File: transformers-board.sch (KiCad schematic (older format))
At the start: 51 parts, among them J1 Screw_Terminal_01x02, J2 Screw_Terminal_01x02, J3 Screw_Terminal_01x02, Q1 IRF3205, U1 UC2844NG4, U2 PC47PQ20_16Z-22

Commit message: Add layout updates
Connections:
- net GNDA: now also C21.2, C23.2; no longer C21.1, C23.1
- net VCCQ: now also C21.1, C23.1; no longer C21.2, C23.2
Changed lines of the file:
@@
 U 1 1 607D6AE4
 P 13725 3825
-F 0 "C20" H 13475 3825 50  0000 L CNN
-F 1 "EEHZA1H101P" H 13150 3925 50  0000 L CNN
+F 0 "C20" H 13450 3825 50  0000 L CNN
+F 1 "EEHZA1H101P" H 13150 3725 50  0000 L CNN
 F 2 "transformers-board:CAPAE1030X1050N" H 13763 3675 50  0001 C CNN
 F 3 "~" H 13725 3825 50  0001 C CNN
@@
 U 1 1 607E1ED3
 P 13950 3825
-F 0 "C21" H 13700 3825 50  0000 L CNN
-F 1 "EEHZA1H101P" H 13350 3725 50  0000 L CNN
+F 0 "C21" H 14075 3825 50  0000 L CNN
+F 1 "EEHZA1H101P" H 14000 3725 50  0000 L CNN
 F 2 "transformers-board:CAPAE1030X1050N" H 13988 3675 50  0001 C CNN
 F 3 "~" H 13950 3825 50  0001 C CNN
 	1    13950 3825
-	-1   0    0    1
+	1    0    0    -1
 $EndComp
 Connection ~ 625  4425
@@
 U 1 1 6082705A
 P 14825 4100
-F 0 "C23" H 14575 4100 50  0000 L CNN
-F 1 "EEHZA1H101P" H 14250 4200 50  0000 L CNN
+F 0 "C23" H 14950 4100 50  0000 L CNN
+F 1 "EEHZA1H101P" H 14850 4000 50  0000 L CNN
 F 2 "transformers-board:CAPAE1030X1050N" H 14863 3950 50  0001 C CNN
 F 3 "~" H 14825 4100 50  0001 C CNN
 	1    14825 4100
-	-1   0    0    1
+	1    0    0    -1
 $EndComp
 $Comp

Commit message: Make changes for Beat's comments
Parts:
- D2, D3, D5, D6, D7: value SL04-E3-08 -> SS2FL4-M3/H
- R7: value 0.75 -> 0.05; PurchasingLink https://www.digikey.com/products/en?keywords=RNCP0805FTD100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 -> https://www.digikey.com/en/products/detail/panasonic-electr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
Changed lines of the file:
@@
 	7000 7850 7000 7500
 Connection ~ 7000 7850
-$Comp
-L Device:D_Schottky D3
-U 1 1 6069B8B4
-P 7000 8475
-F 0 "D3" V 6954 8554 50  0000 L CNN
-F 1 "SL04-E3-08" V 7045 8554 50  0000 L CNN
-F 2 "transformers-board:SODFL3718X108N" H 7000 8475 50  0001 C CNN
-F 3 "~" H 7000 8475 50  0001 C CNN
-	1    7000 8475
-	0    1    1    0
-$EndComp
 Wire Wire Line
 	7000 8625 7000 9250
@@
 	1    7000 6625
 	1    0    0    -1
-$EndComp
-$Comp
-L Device:D_Schottky D2
-U 1 1 606A1A6E
-P 7000 7350
-F 0 "D2" V 6954 7429 50  0000 L CNN
-F 1 "SL04-E3-08" V 7045 7429 50  0000 L CNN
-F 2 "transformers-board:SODFL3718X108N" H 7000 7350 50  0001 C CNN
-F 3 "~" H 7000 7350 50  0001 C CNN
-	1    7000 7350
-	0    1    1    0
 $EndComp
 $Comp
@@
 P 9225 8725
 F 0 "R7" H 9155 8679 50  0000 R CNN
-F 1 "0.75" H 9155 8770 50  0000 R CNN
+F 1 "0.05" H 9155 8770 50  0000 R CNN
 F 2 "footprints:R_0805_OEM" H 8425 8875 50  0001 C CNN
-F 3 "https://www.seielect.com/Catalog/SEI-rncp.pdf" H 8925 9225 50  0001 C CNN
+F 3 "https://industrial.panasonic.com/cdbs/www-data/pdf/RDN0000/AOA0000C313.pdf" H 8925 9225 50  0001 C CNN
 F 4 "DK" H 9225 8725 60  0001 C CNN "MFN"
 F 5 "RNCP0805FTD100RCT-ND" H 8575 8975 60  0001 C CNN "MPN"
-F 6 "https://www.digikey.com/products/en?keywords=RNCP0805FTD100RCT-ND" H 9705 9125 60  0001 C CNN "PurchasingLink"
+F 6 "https://www.digikey.com/en/products/detail/panasonic-electronic-components/ERJ-L06KJ50MV/570932" H 9705 9125 60  0001 C CNN "PurchasingLink"
 	1    9225 8725
 	-1   0    0    1
@@
 Wire Wire Line
 	6850 5250 6850 5450
-$Comp
-L Device:D_Schottky D5
-U 1 1 606A7CB3
-P 7550 4550
-F 0 "D5" H 7600 4725 50  0000 L CNN
-F 1 "SL04-E3-08" H 7595 4629 50  0000 L CNN
-F 2 "transformers-board:SODFL3718X108N" H 7550 4550 50  0001 C CNN
-F 3 "~" H 7550 4550 50  0001 C CNN
-	1    7550 4550
-	1    0    0    -1
-$EndComp
 Wire Wire Line
 	6850 4550 7400 4550
@@
 Wire Wire Line
 	9225 3025 9225 3975
-$Comp
-L Device:D_Schottky D6
-U 1 1 606FF96B
-P 8775 3025
-F 0 "D6" H 8825 3200 50  0000 L CNN
-F 1 "SL04-E3-08" H 8820 3104 50  0000 L CNN
-F 2 "transformers-board:SODFL3718X108N" H 8775 3025 50  0001 C CNN
-F 3 "~" H 8775 3025 50  0001 C CNN
-	1    8775 3025
-	1    0    0    -1
-$EndComp
 Wire Wire Line
 	8625 3025 8250 3025
@@
 Wire Wire Line
 	625  4425 625  4625
-$Comp
-L Device:D_Schottky D7
-U 1 1 6078868E
-P 12000 3475
-F 0 "D7" H 12050 3650 50  0000 L CNN
-F 1 "SL04-E3-08" H 12045 3554 50  0000 L CNN
-F 2 "transformers-board:SODFL3718X108N" H 12000 3475 50  0001 C CNN
-F 3 "~" H 12000 3475 50  0001 C CNN
-	1    12000 3475
-	-1   0    0    1
-$EndComp
 Wire Wire Line
 	11325 3475 11850 3475
@@
 	1    0    0    -1
 $EndComp
+$Comp
+L Device:D_Schottky D7
+U 1 1 6078868E
+P 12000 3475
+F 0 "D7" H 12050 3650 50  0000 L CNN
+F 1 "SS2FL4-M3/H" H 12045 3554 50  0000 L CNN
+F 2 "transformers-board:SODFL3718X108N" H 12000 3475 50  0001 C CNN
+F 3 "https://www.vishay.com/docs/87617/ss2fl4.pdf" H 12000 3475 50  0001 C CNN
+	1    12000 3475
+	-1   0    0    1
+$EndComp
+$Comp
+L Device:D_Schottky D5
+U 1 1 6075E6CB
+P 7550 4550
+F 0 "D5" H 7600 4725 50  0000 L CNN
+F 1 "SS2FL4-M3/H" H 7595 4629 50  0000 L CNN
+F 2 "transformers-board:SODFL3718X108N" H 7550 4550 50  0001 C CNN
+F 3 "https://www.vishay.com/docs/87617/ss2fl4.pdf" H 7550 4550 50  0001 C CNN
+	1    7550 4550
+	1    0    0    -1
+$EndComp
+$Comp
+L Device:D_Schottky D6
+U 1 1 60767520
+P 8775 3025
+F 0 "D6" H 8825 3200 50  0000 L CNN
+F 1 "SS2FL4-M3/H" H 8820 3104 50  0000 L CNN
+F 2 "transformers-board:SODFL3718X108N" H 8775 3025 50  0001 C CNN
+F 3 "https://www.vishay.com/docs/87617/ss2fl4.pdf" H 8775 3025 50  0001 C CNN
+	1    8775 3025
+	1    0    0    -1
+$EndComp
+$Comp
+L Device:D_Schottky D3
+U 1 1 6077F86E
+P 7000 8475
+F 0 "D3" V 6975 8550 50  0000 L CNN
+F 1 "SS2FL4-M3/H" V 7045 8554 50  0000 L CNN
+F 2 "transformers-board:SODFL3718X108N" H 7000 8475 50  0001 C CNN
+F 3 "https://www.vishay.com/docs/87617/ss2fl4.pdf" H 7000 8475 50  0001 C CNN
+	1    7000 8475
+	0    1    1    0
+$EndComp
+$Comp
+L Device:D_Schottky D2
+U 1 1 607A001D
+P 7000 7350
+F 0 "D2" V 6975 7425 50  0000 L CNN
+F 1 "SS2FL4-M3/H" V 7045 7429 50  0000 L CNN
+F 2 "transformers-board:SODFL3718X108N" H 7000 7350 50  0001 C CNN
+F 3 "https://www.vishay.com/docs/87617/ss2fl4.pdf" H 7000 7350 50  0001 C CNN
+	1    7000 7350
+	0    1    1    0
+$EndComp
 $EndSCHEMATC

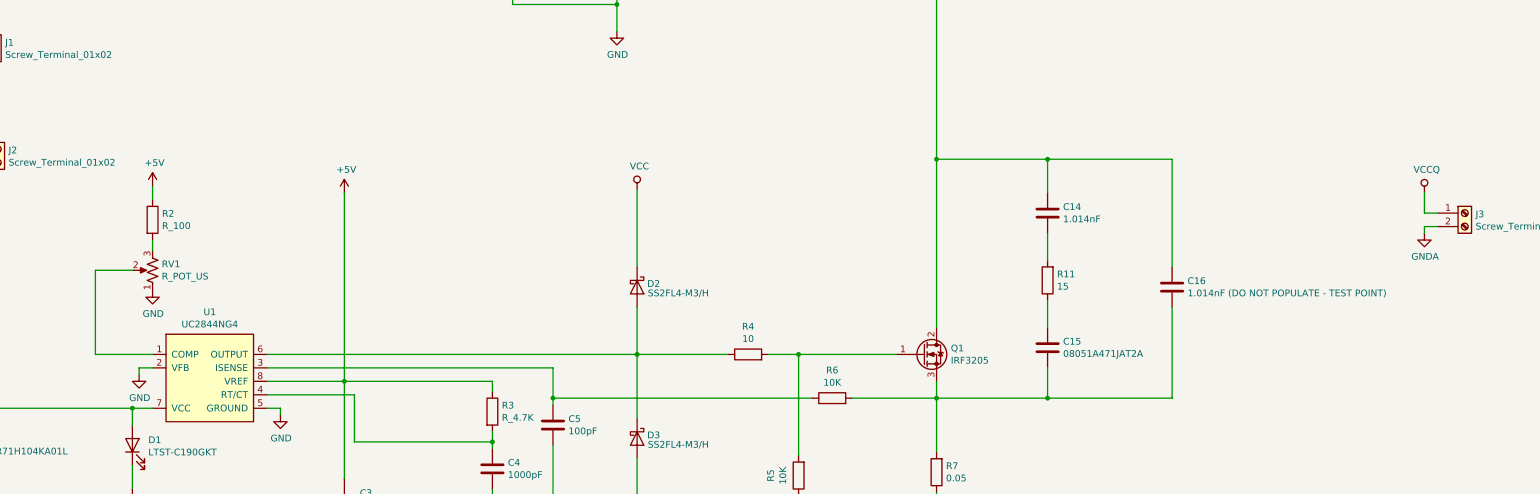
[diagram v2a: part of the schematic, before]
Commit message: Add fabrication outputs
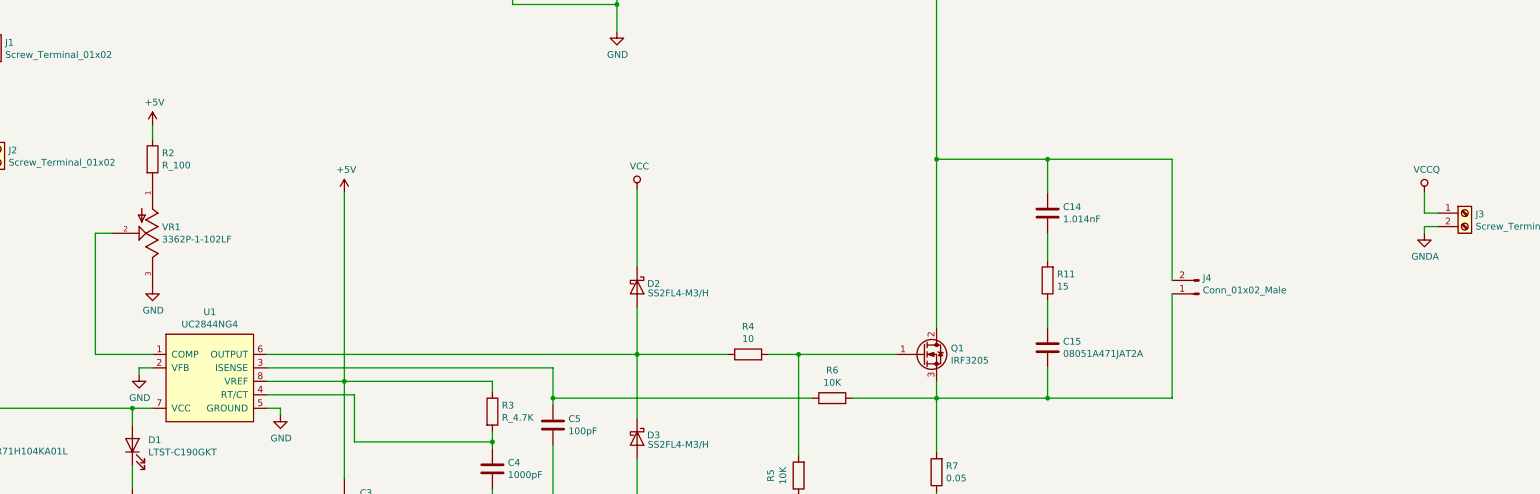
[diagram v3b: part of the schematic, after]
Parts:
- removed C16: 1.014nF (DO NOT POPULATE - TEST POINT), Connector_PinHeader_2.54mm:PinHeader_1x02_P2.54mm_Vertical, symbol Device:C
- removed RV1: R_POT_US, symbol Device:R_POT_US
- added J4: Conn_01x02_Male, Connector_PinHeader_2.54mm:PinHeader_1x02_P2.54mm_Vertical, symbol Connector:Conn_01x02_Male
- added VR1: 3362P-1-102LF, transformers-board:TRIM_3362P-1-102LF, symbol transformers-cc:3362P-1-102LF
- C12: footprint Capacitor_SMD:C_0805_2012Metric -> transformers-board:CAPAE1350X1400N
- C13: footprint Capacitor_SMD:C_0805_2012Metric -> transformers-board:CAPPRD500W60D1000H1800
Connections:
- net GND: now also VR1.3
- net at U1.1 (COMP): now also VR1.2
- net at R2.2: now also VR1.1
- net at C15.2, Q1.3 (S), R6.2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: now also J4.1 (Pin_1)
- net at C14.1, D6.2 (A), Q1.2 (D)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: now also J4.2 (Pin_2)
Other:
- moved on the sheet: R2
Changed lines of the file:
@@
 Wire Wire Line
 	3400 7850 2975 7850
-Wire Wire Line
-	2975 7850 2975 7225
-Wire Wire Line
-	2975 7225 3250 7225
 $Comp
 L power:GND #PWR09
 U 1 1 6066BB95
-P 3400 7375
-F 0 "#PWR09" H 3400 7125 50  0001 C CNN
-F 1 "GND" H 3405 7202 50  0000 C CNN
-F 2 "" H 3400 7375 50  0001 C CNN
-F 3 "" H 3400 7375 50  0001 C CNN
-	1    3400 7375
+P 3400 7350
+F 0 "#PWR09" H 3400 7100 50  0001 C CNN
+F 1 "GND" H 3405 7177 50  0000 C CNN
+F 2 "" H 3400 7350 50  0001 C CNN
+F 3 "" H 3400 7350 50  0001 C CNN
+	1    3400 7350
 	1    0    0    -1
 $EndComp
@@
 	1925 6325 2050 6325
 $Comp
-L Device:R_POT_US RV1
-U 1 1 6067D5A6
-P 3400 7225
-F 0 "RV1" H 3332 7179 50  0000 R CNN
-F 1 "R_POT_US" H 3332 7270 50  0000 R CNN
-F 2 "" H 3400 7225 50  0001 C CNN
-F 3 "~" H 3400 7225 50  0001 C CNN
-	1    3400 7225
-	-1   0    0    1
-$EndComp
-$Comp
 L rocketry:R_100 R2
 U 1 1 6067EB76
-P 3400 6850
-F 0 "R2" H 3470 6896 50  0000 L CNN
-F 1 "R_100" H 3470 6805 50  0000 L CNN
-F 2 "footprints:R_0805_OEM" H 2600 7000 50  0001 C CNN
-F 3 "https://www.seielect.com/Catalog/SEI-rncp.pdf" H 3100 7350 50  0001 C CNN
-F 4 "DK" H 3400 6850 60  0001 C CNN "MFN"
-F 5 "RNCP0805FTD100RCT-ND" H 2750 7100 60  0001 C CNN "MPN"
-F 6 "https://www.digikey.com/products/en?keywords=RNCP0805FTD100RCT-ND" H 3880 7250 60  0001 C CNN "PurchasingLink"
-	1    3400 6850
-	1    0    0    -1
-$EndComp
-Wire Wire Line
-	3400 7000 3400 7075
-Wire Wire Line
-	3400 6600 3400 6700
+P 3400 6400
+F 0 "R2" H 3470 6446 50  0000 L CNN
+F 1 "R_100" H 3470 6355 50  0000 L CNN
+F 2 "footprints:R_0805_OEM" H 2600 6550 50  0001 C CNN
+F 3 "https://www.seielect.com/Catalog/SEI-rncp.pdf" H 3100 6900 50  0001 C CNN
+F 4 "DK" H 3400 6400 60  0001 C CNN "MFN"
+F 5 "RNCP0805FTD100RCT-ND" H 2750 6650 60  0001 C CNN "MPN"
+F 6 "https://www.digikey.com/products/en?keywords=RNCP0805FTD100RCT-ND" H 3880 6800 60  0001 C CNN "PurchasingLink"
+	1    3400 6400
+	1    0    0    -1
+$EndComp
+Wire Wire Line
+	3400 6150 3400 6250
 $Comp
 L power:+5V #PWR08
 U 1 1 6067FED6
-P 3400 6600
-F 0 "#PWR08" H 3400 6450 50  0001 C CNN
-F 1 "+5V" H 3415 6773 50  0000 C CNN
-F 2 "" H 3400 6600 50  0001 C CNN
-F 3 "" H 3400 6600 50  0001 C CNN
-	1    3400 6600
+P 3400 6150
+F 0 "#PWR08" H 3400 6000 50  0001 C CNN
+F 1 "+5V" H 3415 6323 50  0000 C CNN
+F 2 "" H 3400 6150 50  0001 C CNN
+F 3 "" H 3400 6150 50  0001 C CNN
+	1    3400 6150
 	1    0    0    -1
 $EndComp
@@
 Wire Wire Line
 	10050 6400 10975 6400
-Wire Wire Line
-	10975 6400 10975 7200
 Connection ~ 10050 6400
-Wire Wire Line
-	10975 7500 10975 8175
 Wire Wire Line
 	10975 8175 10050 8175
 Connection ~ 10050 8175
-$Comp
-L Device:C C16
-U 1 1 606DF590
-P 10975 7350
-F 0 "C16" H 11090 7396 50  0000 L CNN
-F 1 "1.014nF (DO NOT POPULATE - TEST POINT)" H 11090 7305 50  0000 L CNN
-F 2 "Connector_PinHeader_2.54mm:PinHeader_1x02_P2.54mm_Vertical" H 11013 7200 50  0001 C CNN
-F 3 "~" H 10975 7350 50  0001 C CNN
-	1    10975 7350
-	1    0    0    -1
-$EndComp
 $Comp
 L Connector:Screw_Terminal_01x02 J3
@@
 F 0 "C13" H 6965 5021 50  0000 L CNN
 F 1 "120uF" H 6965 4930 50  0000 L CNN
-F 2 "Capacitor_SMD:C_0805_2012Metric" H 6888 4825 50  0001 C CNN
+F 2 "transformers-board:CAPPRD500W60D1000H1800" H 6888 4825 50  0001 C CNN
 F 3 "~" H 6850 4975 50  0001 C CNN
 	1    6850 4975
@@
 F 0 "C12" H 6965 3446 50  0000 L CNN
 F 1 "200uF" H 6965 3355 50  0000 L CNN
-F 2 "Capacitor_SMD:C_0805_2012Metric" H 6888 3250 50  0001 C CNN
+F 2 "transformers-board:CAPAE1350X1400N" H 6888 3250 50  0001 C CNN
 F 3 "~" H 6850 3400 50  0001 C CNN
 	1    6850 3400
@@
 	0    1    1    0
 $EndComp
+$Comp
+L Connector:Conn_01x02_Male J4
+U 1 1 607C9240
+P 11175 7400
+F 0 "J4" H 11147 7282 50  0000 R CNN
+F 1 "Conn_01x02_Male" H 11147 7373 50  0000 R CNN
+F 2 "Connector_PinHeader_2.54mm:PinHeader_1x02_P2.54mm_Vertical" H 11175 7400 50  0001 C CNN
+F 3 "~" H 11175 7400 50  0001 C CNN
+	1    11175 7400
+	-1   0    0    1
+$EndComp
+Wire Wire Line
+	10975 6400 10975 7300
+Wire Wire Line
+	10975 7400 10975 8175
+$Comp
+L transformers-cc:3362P-1-102LF VR1
+U 1 1 607E6DAD
+P 3400 6950
+F 0 "VR1" V 3354 7020 50  0000 L CNN
+F 1 "3362P-1-102LF" V 3445 7020 50  0000 L CNN
+F 2 "transformers-board:TRIM_3362P-1-102LF" H 3400 6950 50  0001 L BNN
+F 3 "" H 3400 6950 50  0001 L BNN
+F 4 "08/26/10" H 3400 6950 50  0001 L BNN "PARTREV"
+F 5 "3362P-1-205LF" H 3400 6950 50  0001 L BNN "MP"
+F 6 "Bourns" H 3400 6950 50  0001 L BNN "MF"
+F 7 "Manufacturer Recommendation" H 3400 6950 50  0001 L BNN "STANDARD"
+	1    3400 6950
+	0    1    1    0
+$EndComp
+Wire Wire Line
+	2975 6950 3100 6950
+Wire Wire Line
+	2975 6950 2975 7850
 $EndSCHEMATC
